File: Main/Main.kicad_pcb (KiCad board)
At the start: 4 copper layers, 76.2 x 64.9 mm, 78 parts, among them J1 USB_B_Micro, J3 Conn_01x03, J4 Conn_01x03, J5 Conn_01x03, J6 Conn_01x03, J7 MSD-4-A, SW1 SW_Push, SW2 SW_Push, U1 RP2350A-QFN60, U10 LM75B, U11 MCS1802GS-50-Z, U12 MCS1802GS-50-Z, U13 MCS1802GS-50-Z, U14 LM2575-3.3BT, U2 W25Q128JVS, U3 AMS1117-3.3, U4 MMC5983MA, U5 ICM-42688-P, U6 INA226, U7 KX134-1211, U8 MS5611-01BA, U9 MCS1802GS-50-Z, Y1 ABM8-272-T3

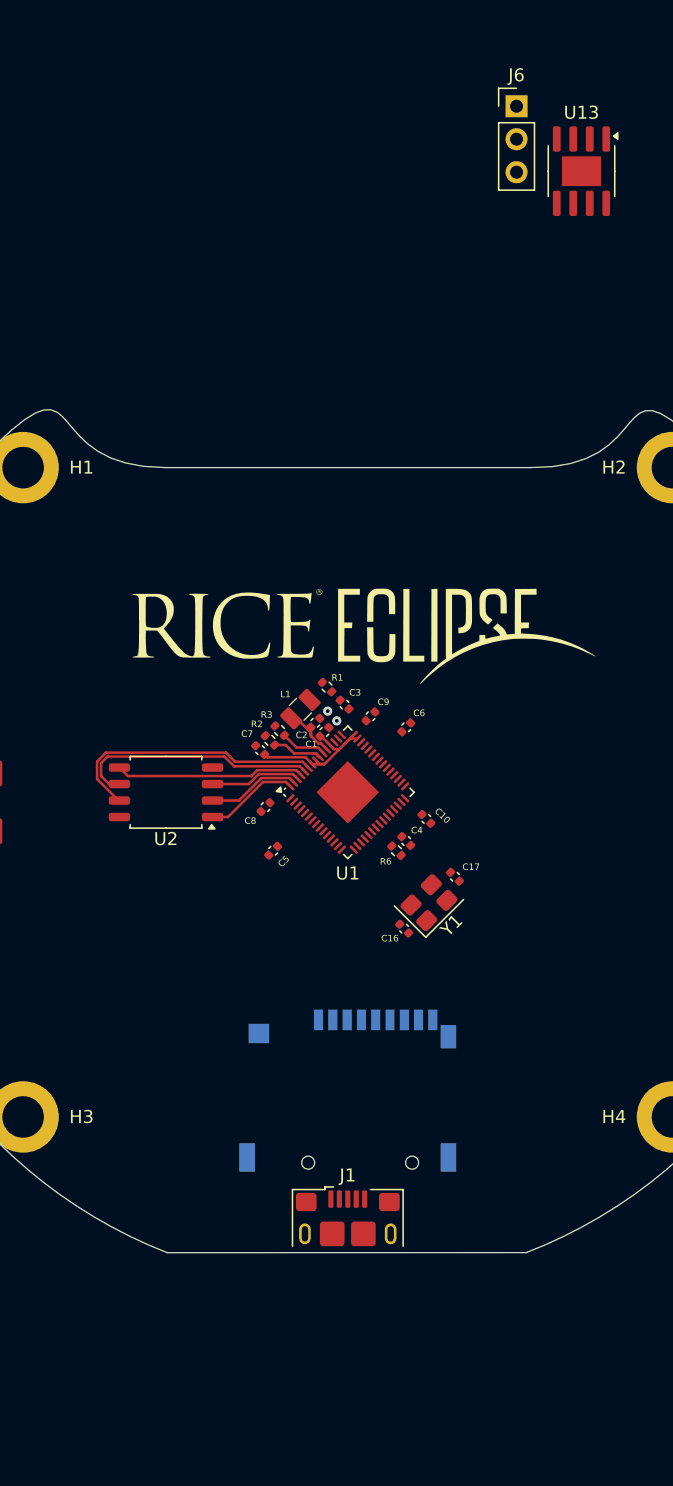
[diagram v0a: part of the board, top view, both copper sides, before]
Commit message: added xt60 connector
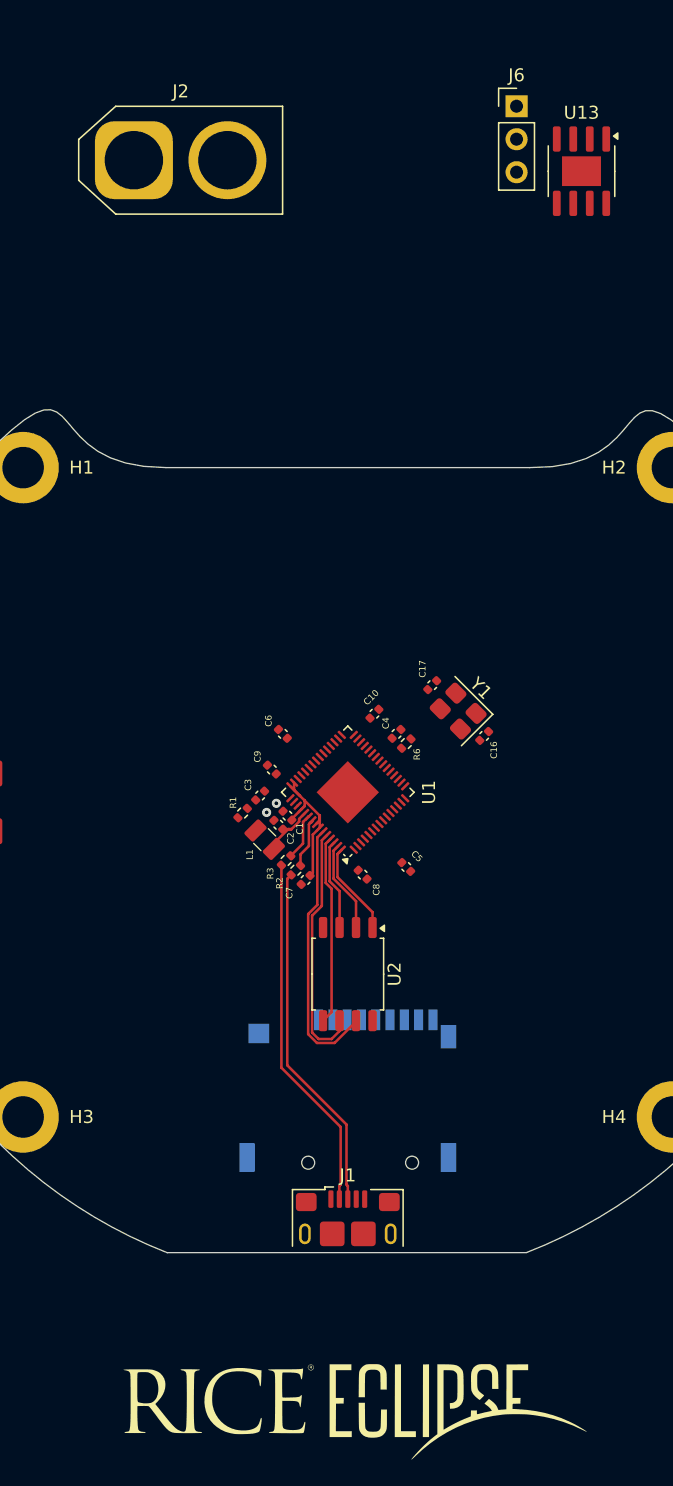
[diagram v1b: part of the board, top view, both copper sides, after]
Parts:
- added J2: Conn_01x02, Connector_AMASS:AMASS_XT60-M_1x02_P7.20mm_Vertical, F.Cu at (83.5, 51.3)
- moved G*** 59.7 mm to (100.6, 147.5)
- moved U2 19.8 mm to (100.0, 114.0), turned to -90 degrees
- moved C16 16.1 mm to (110.5, 95.7), turned to 45 degrees
- moved Y1 14.9 mm to (108.5, 93.8), turned to 135 degrees
- moved C17 14.9 mm to (106.5, 91.8), turned to -135 degrees
- moved R1 11.7 mm to (91.9, 101.6), turned to 45 degrees
- moved C7 10.6 mm to (96.8, 106.8), turned to -135 degrees
- moved L1 10.4 mm to (93.6, 103.7), turned to 135 degrees
- moved C5 10.3 mm to (104.5, 105.8), turned to -45 degrees
- moved R2 10.2 mm to (96.0, 106.0), turned to -135 degrees
- moved R3 10.0 mm to (95.2, 105.2), turned to -135 degrees
- moved C3 9.55 mm to (93.2, 100.2), turned to 45 degrees
- moved C6 9.51 mm to (95.0, 95.5), turned to 135 degrees
- moved C8 9.11 mm to (101.1, 106.3), turned to -45 degrees
- moved C10 9.03 mm to (102.0, 94.0), turned to 45 degrees
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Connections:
- U14 pad 4: VOUT -> +3.3V
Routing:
- net /USB_D-: track 0.00 -> 27.6 mm
- net /USB_D+: track 0.00 -> 27.0 mm

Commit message: ready for schematic planning
still no sd card circuit/components for regulator but we can plan more where everything goes
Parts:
- moved U14 11.4 mm to (67.9, 25.8)
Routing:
- net /USB_D+: track 27.0 -> 15.9 mm
- net /USB_D-: track 27.6 -> 16.9 mm
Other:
- board text added: "this box estimates total footprint size of switching voltage regulator use for planning"
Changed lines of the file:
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@@
 	(footprint "Package_TO_SOT_SMD:TO-263-5_TabPin3"
 		(layer "F.Cu")
-		(at 61.4 35.15)
+		(at 67.925 25.775)
 		(descr "TO-263/D2PAK/DDPAK SMD package, http://www.infineon.com/cms/en/product/packages/PG-TO263/PG-TO263-5-1/")
 		(tags "D2PAK DDPAK TO-263 D2PAK-5 TO-263-5 SOT-426")
@@
 		)
 	)
+	(gr_rect
+		(start 55 17.5)
+		(end 90 40.5)
+		(stroke
+			(width 0.1)
+			(type default)
+		)
+		(fill no)
+		(layer "F.SilkS")
+	)
 	(gr_curve
 		(pts
@@
 		(layer "Edge.Cuts")
 	)
+	(gr_text "this box estimates total footprint size of switching voltage regulator\nuse for planning\n"
+		(at 56 16 0)
+		(layer "F.SilkS")
+		(effects
+			(font
+				(size 1 1)
+				(thickness 0.1)
+			)
+			(justify left bottom)
+		)
+	)
 	(segment
 		(start 96.68109 101.056169)
@@
 	)
 	(segment
-		(start 99.9 125.581802)
-		(end 99.9 130.212499)
+		(start 95.639376 106.360624)
+		(end 95.339377 106.660623)
 		(width 0.2)
 		(layer "F.Cu")
@@
 	(segment
 		(start 95.339377 121.021179)
-		(end 99.9 125.581802)
-		(width 0.2)
-		(layer "F.Cu")
-		(net 25)
-	)
-	(segment
-		(start 99.9 130.212499)
-		(end 100 130.312499)
-		(width 0.2)
-		(layer "F.Cu")
-		(net 25)
-	)
-	(segment
-		(start 95.639376 106.360624)
-		(end 95.339377 106.660623)
+		(end 96.159099 121.840901)
 		(width 0.2)
 		(layer "F.Cu")
@@
 	)
 	(segment
-		(start 100 130.312499)
-		(end 100 131.325)
-		(width 0.2)
-		(layer "F.Cu")
-		(net 25)
-	)
-	(segment
-		(start 94.889376 105.610624)
-		(end 94.889376 121.207574)
-		(width 0.2)
-		(layer "F.Cu")
-		(net 26)
-	)
-	(segment
 		(start 94.889376 121.207574)
-		(end 99.45 125.768198)
-		(width 0.2)
-		(layer "F.Cu")
-		(net 26)
-	)
-	(segment
-		(start 99.45 125.768198)
-		(end 99.45 130.212499)
+		(end 95.840901 122.159099)
 		(width 0.2)
 		(layer "F.Cu")
@@
 	)
 	(segment
-		(start 99.35 130.312499)
-		(end 99.35 131.325)
-		(width 0.2)
-		(layer "F.Cu")
-		(net 26)
-	)
-	(segment
-		(start 99.45 130.212499)
-		(end 99.35 130.312499)
+		(start 94.889376 105.610624)
+		(end 94.889376 121.207574)
 		(width 0.2)
 		(layer "F.Cu")

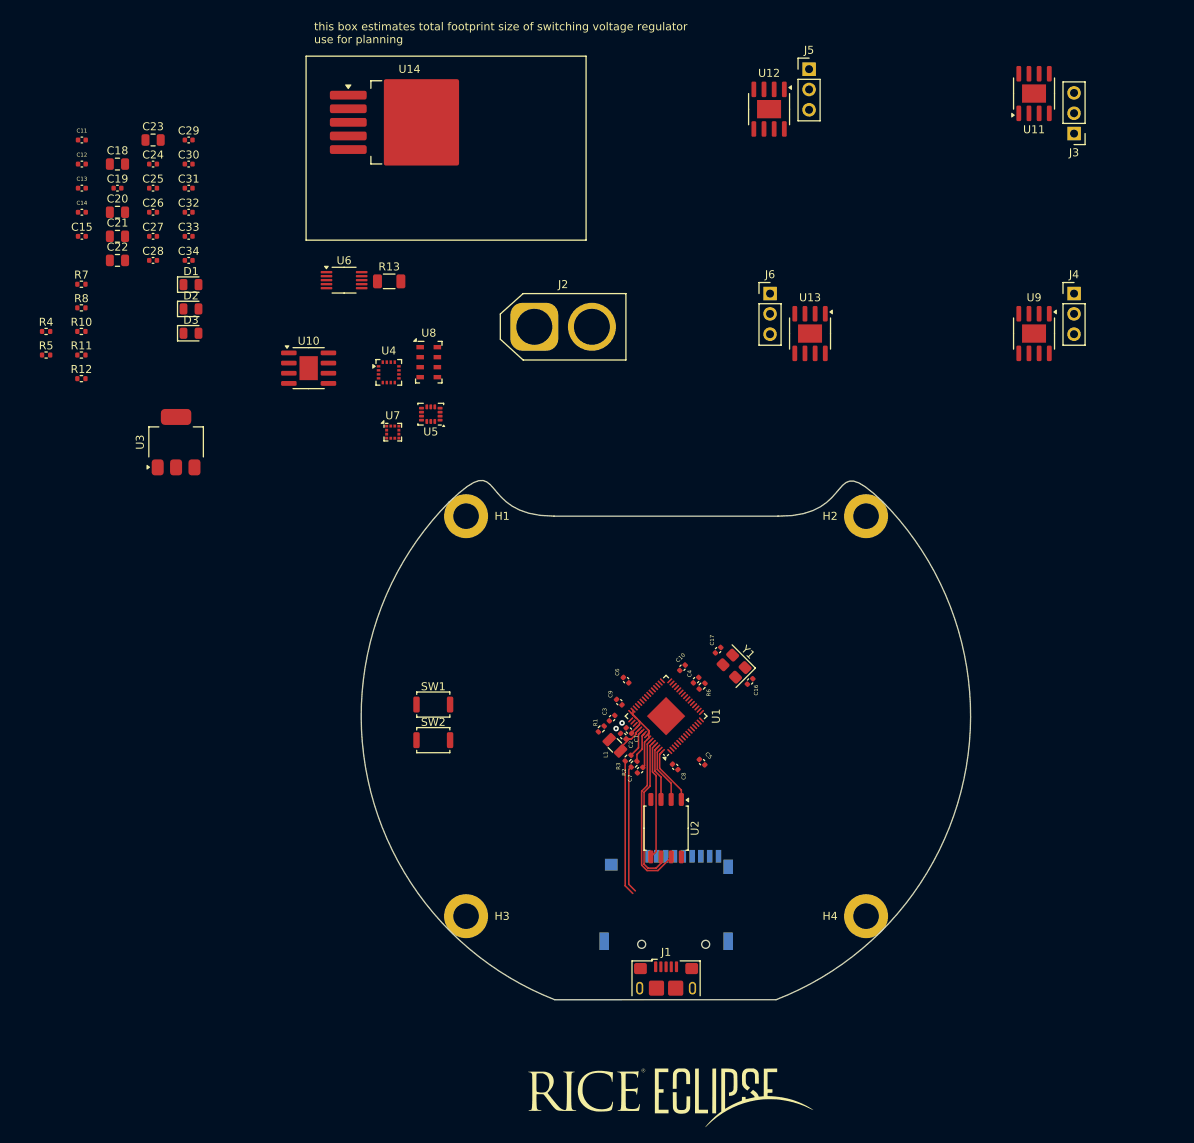
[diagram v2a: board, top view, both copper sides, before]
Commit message: added p-channel mosfet for power control
USB plugged in -> VBUS high, Vgs on mosfet = 0 -> mosfet off, disconect linear regulator from 3.3v system rails
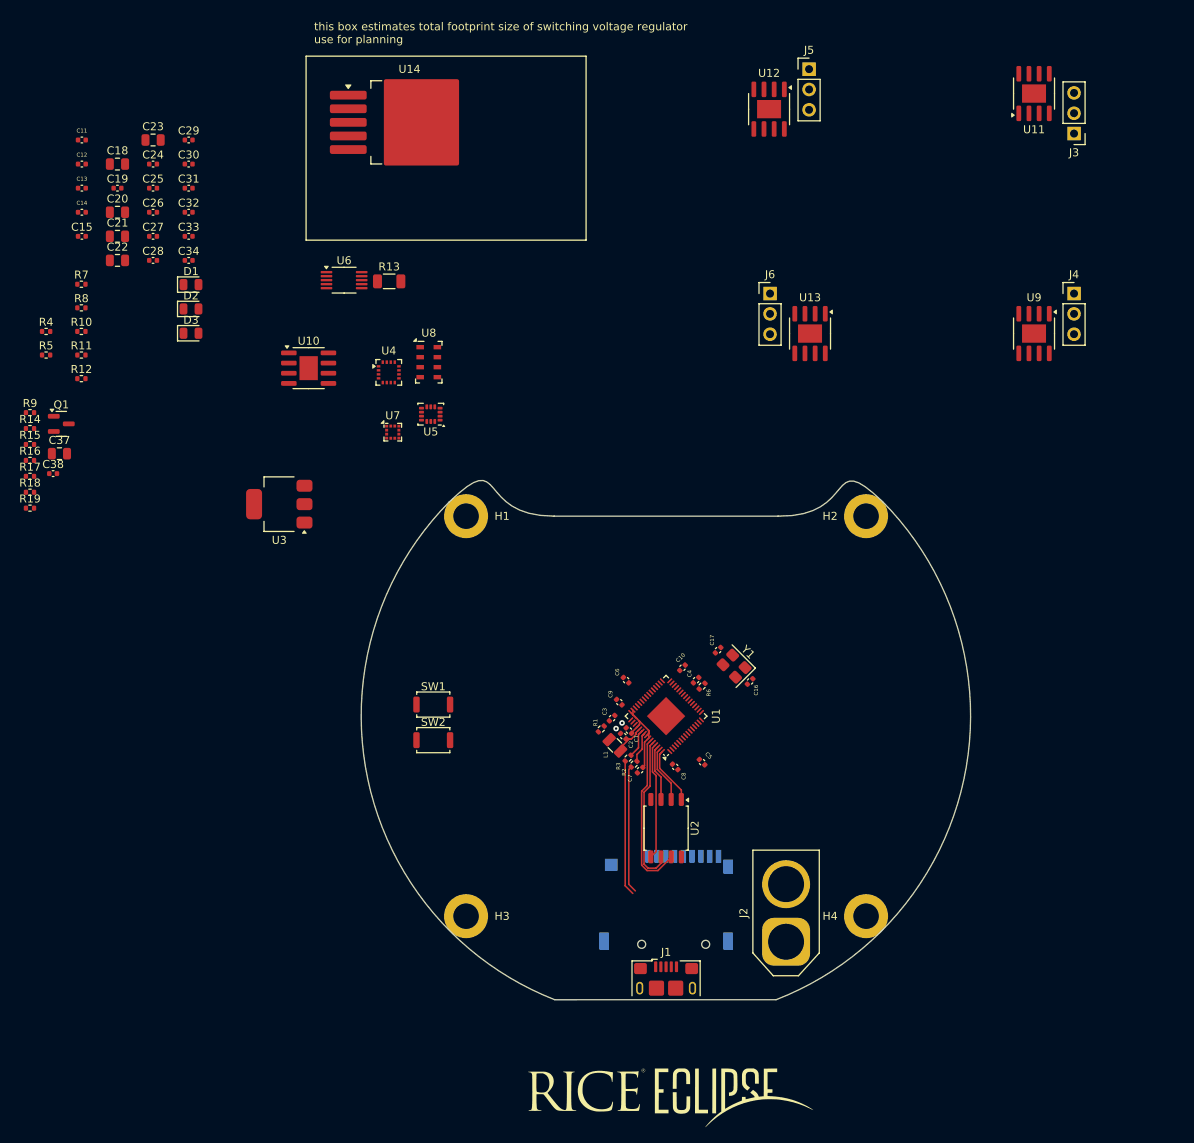
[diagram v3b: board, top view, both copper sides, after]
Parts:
- added C37: 10u, Capacitor_SMD:C_0805_2012Metric, F.Cu at (24.2, 67.2)
- added C38: 100n, Capacitor_SMD:C_0402_1005Metric, F.Cu at (23.4, 69.7)
- added Q1: Si2301CDS, Package_TO_SOT_SMD:SOT-23, F.Cu at (24.4, 63.5)
- added R14: 10k, Resistor_SMD:R_0402_1005Metric, F.Cu at (20.5, 64.0)
- added R15: 10k, Resistor_SMD:R_0402_1005Metric, F.Cu at (20.5, 66.0)
- added R16: 10k, Resistor_SMD:R_0402_1005Metric, F.Cu at (20.5, 68.0)
- added R17: 10k, Resistor_SMD:R_0402_1005Metric, F.Cu at (20.5, 70.0)
- added R18: 10k, Resistor_SMD:R_0402_1005Metric, F.Cu at (20.5, 72.0)
- added R19: 100k, Resistor_SMD:R_0402_1005Metric, F.Cu at (20.5, 74.0)
- added R9: 10k, Resistor_SMD:R_0402_1005Metric, F.Cu at (20.5, 62.1)
- moved J2 83.1 mm to (115.0, 128.2), turned to 90 degrees
- moved U3 15.0 mm to (51.6, 73.5), turned to 180 degrees
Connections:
- J7 pad 1: unconnected-(J7-DAT2-Pad1) -> Net-(J7-DAT2)
- J7 pad 2: unconnected-(J7-CD/DAT3-Pad2) -> SD_ChipSelect
- J7 pad 3: unconnected-(J7-CMD-Pad3) -> SPI_SDI2
- J7 pad 4: unconnected-(J7-VDD-Pad4) -> +3.3V
- J7 pad 5: unconnected-(J7-CLK-Pad5) -> SPI_SCLK2
- J7 pad 6: unconnected-(J7-VSS-Pad6) -> GND
- J7 pad 7: unconnected-(J7-DAT0-Pad7) -> SPI_SDO2
- J7 pad 8: unconnected-(J7-DAT1-Pad8) -> Net-(J7-DAT1)
- J7 pad CD: unconnected-(J7-PadCD) -> SD_CD
- J7 pad G1: unconnected-(J7-COVER_GND-PadG1) -> GND
- J7 pad G2: unconnected-(J7-COVER_GND__1-PadG2) -> GND
- J7 pad G3: unconnected-(J7-COVER_GND__2-PadG3) -> GND
- J7 pad G4: unconnected-(J7-COVER_GND__3-PadG4) -> GND
- U11 pad 1: current + -> VIN
- U11 pad 2: current + -> VIN
- U12 pad 1: current -3 -> VIN
- U12 pad 2: current -3 -> VIN
- U13 pad 1: current + -> VIN
- U13 pad 2: current + -> VIN
- U14 pad 4: +3.3V -> Net-(Q1-S)
- U9 pad 1: current -2 -> VIN
- U9 pad 2: current -2 -> VIN

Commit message: changed voltage regulator
new voltage regulator chip(smaller + more effecient) and supporting components
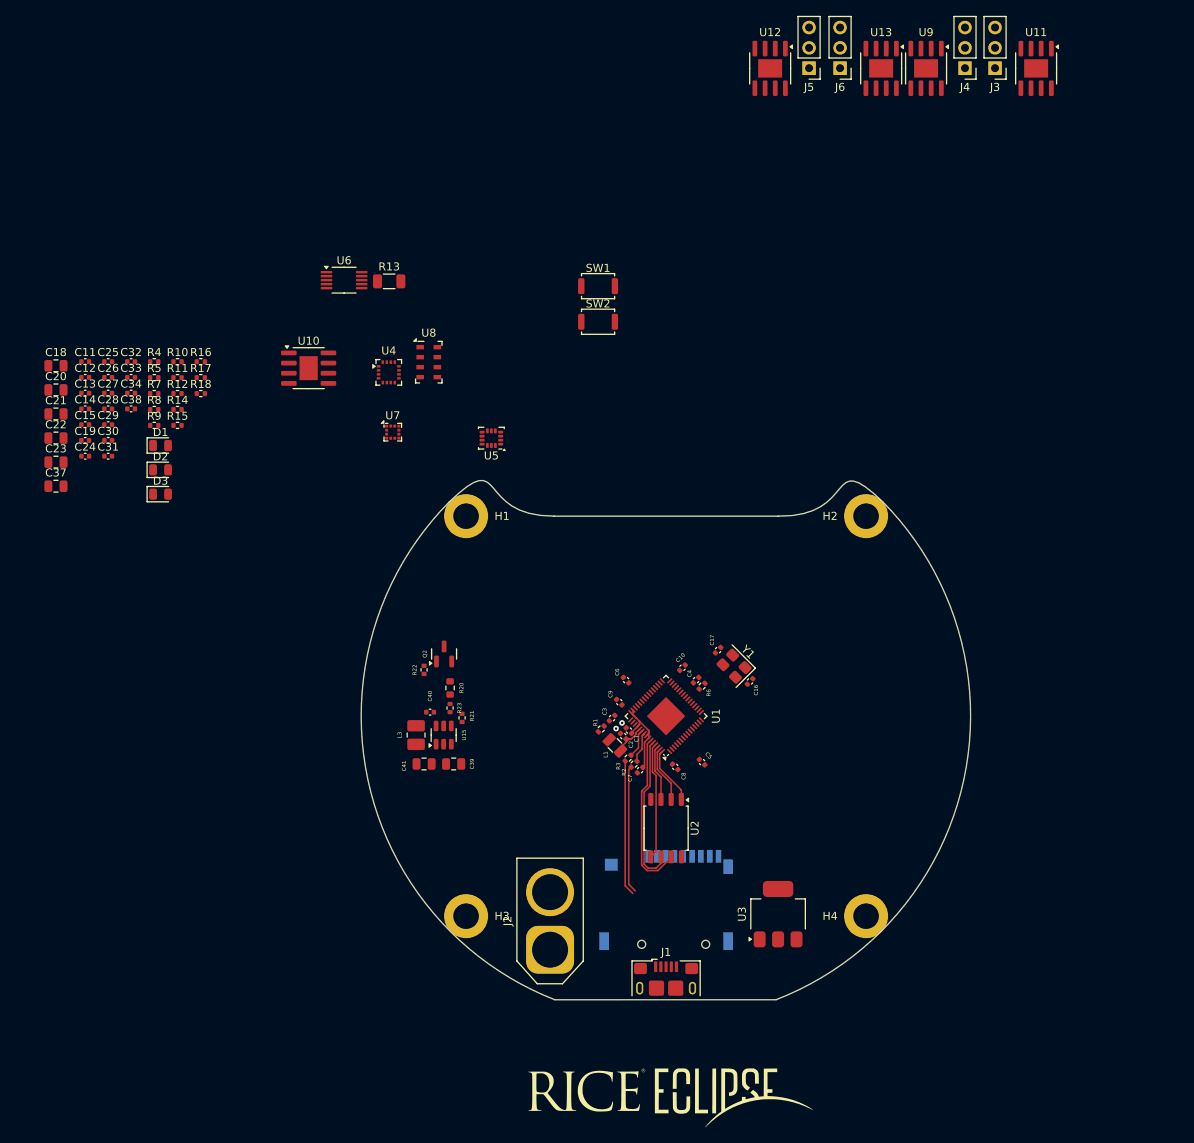
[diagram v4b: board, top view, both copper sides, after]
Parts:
- removed Q1: Si2301CDS, Package_TO_SOT_SMD:SOT-23
- removed R19: 100k, Resistor_SMD:R_0402_1005Metric
- removed U14: LM2575-3.3BT, Package_TO_SOT_SMD:TO-263-5_TabPin3
- added C39: 10u, Capacitor_SMD:C_0805_2012Metric, F.Cu at (73.5, 106.0)
- added C40: 100n, Capacitor_SMD:C_0402_1005Metric, F.Cu at (70.5, 99.5)
- added C41: 22u, Capacitor_SMD:C_0805_2012Metric, F.Cu at (69.8, 106.0)
- added L3: 3.3u, Inductor_SMD:L_1008_2520Metric_Pad1.43x2.20mm_HandSolder, F.Cu at (68.8, 102.4)
- added Q2: Si2301CDS, Package_TO_SOT_SMD:SOT-23, F.Cu at (72.2, 92.2)
- added R20: 30k, Resistor_SMD:R_0603_1608Metric, F.Cu at (73.0, 96.5)
- added R21: 10k, Resistor_SMD:R_0402_1005Metric, F.Cu at (74.5, 100.2)
- added R22: 100k, Resistor_SMD:R_0402_1005Metric, F.Cu at (69.8, 94.2)
- added R23: 1k, Resistor_SMD:R_0402_1005Metric, F.Cu at (73.0, 99.0)
- added U15: AP62150WU, Package_TO_SOT_SMD:TSOT-23-6, F.Cu at (72.2, 102.4)
- J2: value Conn_01x02 -> XT60
- moved U3 80.7 mm to (114.0, 124.8), turned to 90 degrees
- moved SW1 56.2 mm to (91.5, 46.2)
- moved SW2 56.2 mm to (91.5, 50.7)
- moved C23 42.1 mm to (23.7, 68.2)
- moved C24 37.5 mm to (27.4, 67.5)
- moved C29 37.0 mm to (30.3, 63.6)
- moved C30 36.0 mm to (30.3, 65.5)
- moved U9 35.8 mm to (132.5, 19.0)
- moved C31 35.0 mm to (30.3, 67.5)
- moved U13 34.3 mm to (126.9, 19.0)
- moved C19 31.8 mm to (27.4, 65.5)
- moved J4 31.3 mm to (137.4, 19.0), turned to 180 degrees
- moved J2 29.5 mm to (85.5, 129.2)
- moved J6 29.5 mm to (121.8, 19.0), turned to 180 degrees
- moved C11 27.7 mm to (27.4, 55.7)
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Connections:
- U12 pad 1: VIN -> current -3
- U12 pad 2: VIN -> current -3
- U12 pad 3: current + -> VIN
- U12 pad 4: current + -> VIN
- U9 pad 1: VIN -> current -2
- U9 pad 2: VIN -> current -2
- U9 pad 3: current + -> VIN
- U9 pad 4: current + -> VIN
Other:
- board text removed: "this box estimates total footprint size of switching voltage regulator use for planning"

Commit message: some layout stuff
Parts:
- moved C20 117.1 mm to (116.5, 130.8), turned to 180 degrees
- moved C21 108.4 mm to (110.2, 127.5), turned to 90 degrees
- moved U13 69.7 mm to (97.0, 82.0)
- moved J6 69.7 mm to (92.0, 82.0)
- moved U11 69.6 mm to (116.5, 82.0)
- moved J3 69.6 mm to (111.5, 82.0)
- moved U12 69.5 mm to (83.5, 82.0)
- moved U9 69.5 mm to (103.0, 82.0)
- moved J5 69.5 mm to (88.5, 82.0)
- moved J4 69.5 mm to (108.0, 82.0)
- moved R13 68.9 mm to (80.2, 112.9)
- moved U6 68.9 mm to (74.5, 112.8)
- moved G*** 58.0 mm to (100.0, 89.5)
- moved R22 13.8 mm to (81.6, 101.2), turned to 180 degrees
- moved Q2 9.83 mm to (79.6, 98.8), turned to 180 degrees
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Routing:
- net VBUS: track 0.00 -> 21.6 mm
- net /USB_D-: track 16.9 -> 12.9 mm
- net /USB_D+: track 15.9 -> 12.3 mm
